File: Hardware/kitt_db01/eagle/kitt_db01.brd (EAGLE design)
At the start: 74.3 x 53.3 mm, 25 parts, among them Q1 [MMBF170], U1 ADNS-3080, U2 MIC5205-3.3YM5TR, X1 RESON

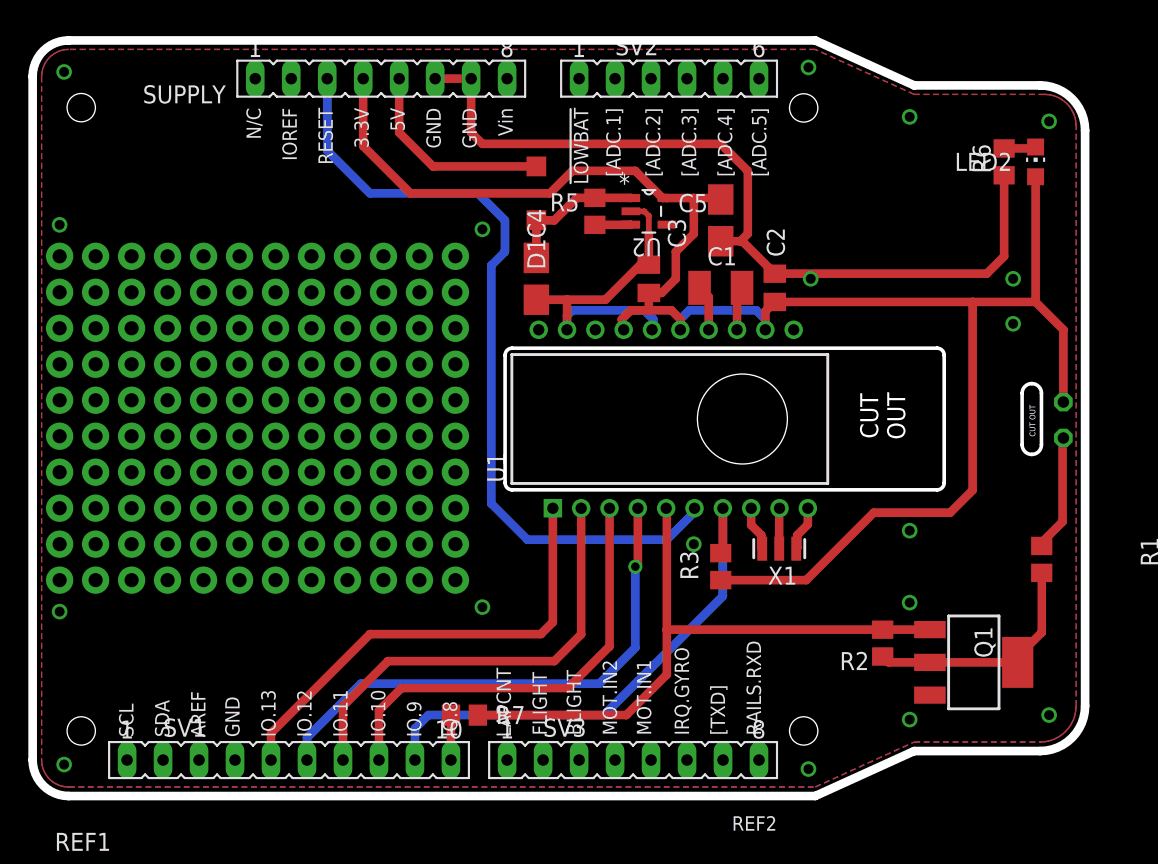
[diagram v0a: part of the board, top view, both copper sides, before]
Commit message: board snapshot of db01 + added patching area for north-west port
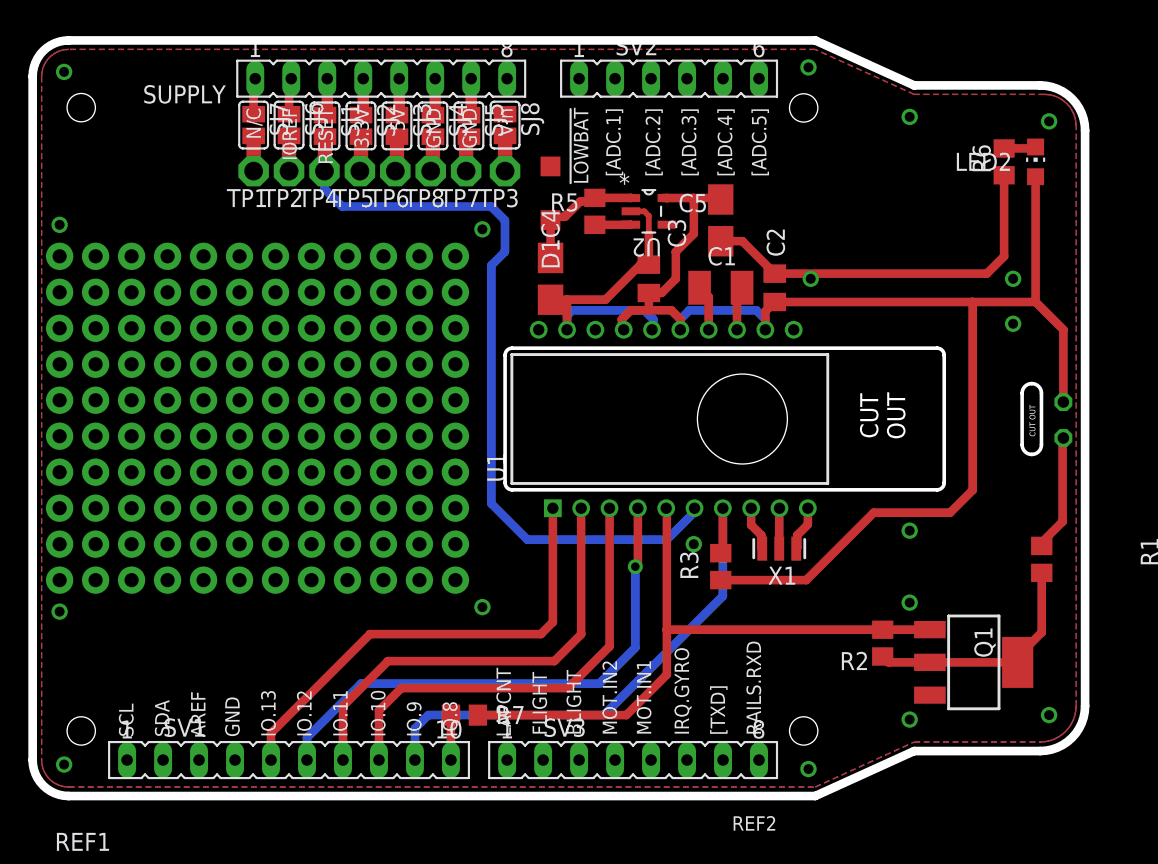
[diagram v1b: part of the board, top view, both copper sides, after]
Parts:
- added SJ1, SJ2, SJ3, SJ4, SJ5, SJ6, SJ7, SJ8: (no value), jumper:SJ
- added TP1, TP2, TP3, TP4, TP5, TP6, TP7, TP8: TPPAD1-13, testpad:P1-13
- moved C4 1.00 mm to (30.2, 68.9)
- moved D1 1.00 mm to (30.2, 74.9)
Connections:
- new net N$12: SJ1.1, SUPPLY.3
- new net N$13: SJ2.1, SUPPLY.4
- new net N$134: SJ3.1, SUPPLY.5
- new net N$135: SJ4.1, SUPPLY.6
- new net N$136: SJ5.1, SUPPLY.7
- new net N$137: SJ7.1, SUPPLY.1
- new net N$138: SJ6.1, SUPPLY.2
- new net N$139: SJ8.1, SUPPLY.8
- new net N$140: SJ7.2, TP1.TP
- new net N$141: SJ6.2, TP2.TP
- new net N$142: SJ8.2, TP3.TP
- net +3V3: now also SJ2.2, TP5.TP; no longer SUPPLY.4
- net +5V: now also SJ3.2, TP6.TP; no longer SUPPLY.5
- net GND: now also SJ4.2, SJ5.2, TP7.TP, TP8.TP; no longer SUPPLY.6, SUPPLY.7
- net RST: now also SJ1.2, TP4.TP; no longer SUPPLY.3
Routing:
- net GND: track 83.6 -> 55.1 mm
- net +3V3: track 128.3 -> 102.1 mm
- net +5V: track 14.5 -> 2.48 mm
- net N$135: track 0.00 -> 2.64 mm
- net N$134: track 0.00 -> 2.64 mm
- net N$12: track 0.00 -> 2.64 mm
- net N$136: track 0.00 -> 2.64 mm
- net N$13: track 0.00 -> 2.64 mm
- net N$138: track 0.00 -> 2.58 mm
- net N$137: track 0.00 -> 2.56 mm
- net N$142: track 0.00 -> 2.49 mm
- net N$141: track 0.00 -> 2.49 mm
- net N$140: track 0.00 -> 2.49 mm
- net RST: track 56.5 -> 54.3 mm
- net N$9: track 9.99 -> 8.99 mm
- added copper zone on layer 3, net GND

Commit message: snapshot of board db01 + added southwest patching area
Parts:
- added SJ10, SJ11, SJ12, SJ13, SJ14, SJ15, SJ16, SJ17, SJ18, SJ19, SJ9: (no value), jumper:SJ
- added TP10, TP11, TP12, TP13, TP14, TP15, TP16, TP17, TP18, TP9: TPPAD1-13, testpad:P1-13
- moved R7 5.25 mm to (29.4, 38.1)
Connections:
- new net N$143: SJ9.1, SV1.1
- new net N$144: SJ10.1, SV1.2
- new net N$145: SJ11.1, SV1.3
- new net N$146: SJ11.2, TP9.TP
- new net N$147: SJ12.1, SV1.4
- new net N$148: SJ13.1, SV1.5
- new net N$149: SJ14.1, SV1.6
- new net N$150: SJ15.1, SV1.7
- new net N$151: SJ16.1, SV1.8
- new net N$152: SJ17.1, SV1.9
- new net N$153: SJ18.1, SV1.10
- new net SCL: SJ9.2, TP11.TP
- new net SDA: SJ10.2, TP10.TP
- net !CS: now also SJ13.2, TP12.TP; no longer SV1.5
- net !LEDCTRL: now also SJ18.2, TP17.TP; no longer SV1.10
- net !PD: now also SJ17.2, TP16.TP; no longer SV1.9
- net GND: now also SJ12.2, TP18.TP; no longer SV1.4
- net MISO: now also SJ15.2, TP14.TP; no longer SV1.7
- net MOSI: now also SJ14.2, TP13.TP; no longer SV1.6
- net SCLK: now also SJ16.2, TP15.TP; no longer SV1.8
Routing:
- net MOSI: track 37.3 -> 15.7 mm
- net MISO: track 31.6 -> 13.8 mm
- net SCLK: track 31.4 -> 16.2 mm
- net !PD: track 37.3 -> 24.9 mm
- net !CS: track 33.1 -> 23.5 mm
- net N$4: track 44.9 -> 39.6 mm
- net N$153: track 0.00 -> 2.64 mm
- net N$152: track 0.00 -> 2.62 mm
- net N$144: track 0.00 -> 2.61 mm
- net N$145: track 0.00 -> 2.61 mm
- net N$151: track 0.00 -> 2.60 mm
- net N$143: track 0.00 -> 2.59 mm
- net N$147: track 0.00 -> 2.59 mm
- net N$150: track 0.00 -> 2.59 mm
- net N$139: track 0.00 -> 2.57 mm
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
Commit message: snapshot of db01 board -> added northeast and southeast patchthough to pins
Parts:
- added SJ20, SJ21, SJ22, SJ23, SJ24, SJ25, SJ26, SJ27, SJ28, SJ29, SJ30, SJ31, SJ32, SJ33: (no value), jumper:SJ
- added TP19, TP20, TP21, TP22, TP23, TP24, TP25, TP26, TP27, TP28, TP29, TP30, TP31, TP32: TPPAD1-13, testpad:P1-13
- moved SJ19 16.8 mm to (65.2, 28.0)
- moved R7 8.07 mm to (31.6, 45.9)
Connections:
- new net N$154: SJ20.1, SV2.6
- new net N$155: SJ21.1, SV2.5
- new net N$156: SJ22.1, SV2.4
- new net N$157: SJ23.1, SV2.3
- new net N$158: SJ24.1, SV2.2
- new net N$159: SJ25.1, SV2.1
- new net N$160: SJ26.1, SV3.8
- new net N$161: SJ27.1, SV3.7
- new net N$162: SJ28.1, SV3.6
- new net N$163: SJ29.1, SV3.5
- new net N$164: SJ30.1, SV3.4
- new net N$165: SJ31.1, SV3.3
- new net N$166: SJ32.1, SV3.2
- new net N$167: SJ33.1, SV3.1
- new net N$168: SJ20.2, TP19.TP
- new net N$169: SJ21.2, TP20.TP
- new net N$170: SJ22.2, TP21.TP
- new net N$171: SJ23.2, TP22.TP
- new net N$172: SJ24.2, TP23.TP
- new net N$173: SJ25.2, TP24.TP
- new net N$174: SJ26.2, TP25.TP
- new net N$175: SJ27.2, TP26.TP
- new net N$176: SJ28.2, TP27.TP
- new net N$177: SJ29.2, TP28.TP
- new net N$178: SJ30.2, TP29.TP
- new net N$179: SJ31.2, TP30.TP
- new net N$180: SJ32.2, TP31.TP
- new net N$181: SJ33.2, TP32.TP
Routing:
- net !CS: track 23.5 -> 2.24 mm
- net SCLK: track 16.2 -> 2.24 mm
- net N$4: track 39.6 -> 27.2 mm
- net !PD: track 24.9 -> 13.0 mm
- net MISO: track 13.8 -> 2.24 mm
- net MOSI: track 15.7 -> 6.43 mm
- net N$160: track 0.00 -> 2.64 mm
- net N$161: track 0.00 -> 2.62 mm
- net N$167: track 0.00 -> 2.61 mm
- net N$162: track 0.00 -> 2.60 mm
- net N$166: track 0.00 -> 2.59 mm
- net N$154: track 0.00 -> 2.59 mm
- net N$163: track 0.00 -> 2.59 mm
- net N$165: track 0.00 -> 2.57 mm
- net N$155: track 0.00 -> 2.57 mm
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
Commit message: snapshot of db01 board layout -> added alternate LEDs for illuminating surface
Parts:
- removed Q1: [MMBF170], transistor-power:SOT223
- removed SJ19: (no value), jumper:SJ
- added LED3, LED4, LED5: (no value), led:CHIP-LED0805
- added R10, R9: 330R, rcl:R0805
- added R4: [0R], rcl:R0805
- added U9.01: SI1922EDH, kitt.ic:SC70-6
- moved R2 11.0 mm to (61.0, 51.4)
- moved R7 5.10 mm to (36.5, 47.3), turned to 270 degrees
- moved R1 2.40 mm to (65.1, 46.7)
- moved R5 1.91 mm to (33.3, 71.8)
- moved R3 1.27 mm to (42.2, 47.3)
- moved U2 1.27 mm to (37.1, 72.4)
- moved C5 0.95 mm to (42.2, 72.1), turned to 180 degrees
- moved LED1 0.63 mm to (65.8, 58.9)
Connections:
- new net N$184: R4.2, U9.01.5
- new net N$185: LED4.C, R9.2
- new net N$186: R10.1, R9.1, U9.01.3
- new net N$187: LED5.C, R10.2
- net !LEDCTRL: now also R4.1
- net +3V3: now also LED3.A, LED4.A, LED5.A
- net GND: now also U9.01.1, U9.01.4; no longer Q1.3
- net MISO: now also SJ14.2, TP13.TP; no longer SJ15.2, TP14.TP
- net MOSI: now also SJ16.2, TP15.TP; no longer SJ14.2, TP13.TP
- net N$4: now also U9.01.2; no longer Q1.1
- net N$7: now also U9.01.6; no longer Q1.2, Q1.4
- net N$8: now also LED3.C
- net SCLK: now also SJ15.2, TP14.TP; no longer SJ16.2, TP15.TP
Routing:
- net +3V3: track 102.1 -> 131.2 mm, vias 0 -> 4
- net !CS: track 2.24 -> 29.3 mm
- net MISO: track 2.24 -> 28.4 mm, vias 0 -> 1
- net SCLK: track 2.24 -> 26.9 mm
- net !PD: track 13.0 -> 36.0 mm
- net MOSI: track 6.43 -> 27.0 mm, vias 1 -> 0
- net N$7: track 16.7 -> 0.00 mm
- net !LEDCTRL: track 2.24 -> 18.8 mm, vias 0 -> 1
- net +5V: track 2.48 -> 16.7 mm
- net GND: track 55.1 -> 41.5 mm, vias 18 -> 15
- net N$4: track 27.2 -> 18.0 mm
- net N$8: track 8.23 -> 1.75 mm
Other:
- board size 74.3 x 53.3 mm -> 133.3 x 98.3 mm
- board text added: "40deg light cone"
- board text added: "80deg light cone"
- board text added: "<-- replace with SMT LED (there's got to be one, no need for shite slot)"
- board text added: "or atleast an alternate footprint"
- board text removed: "The Prototyping Area is here because: - it enables quick bodgejobs - it uses up real estate which would be wasted otherwise"

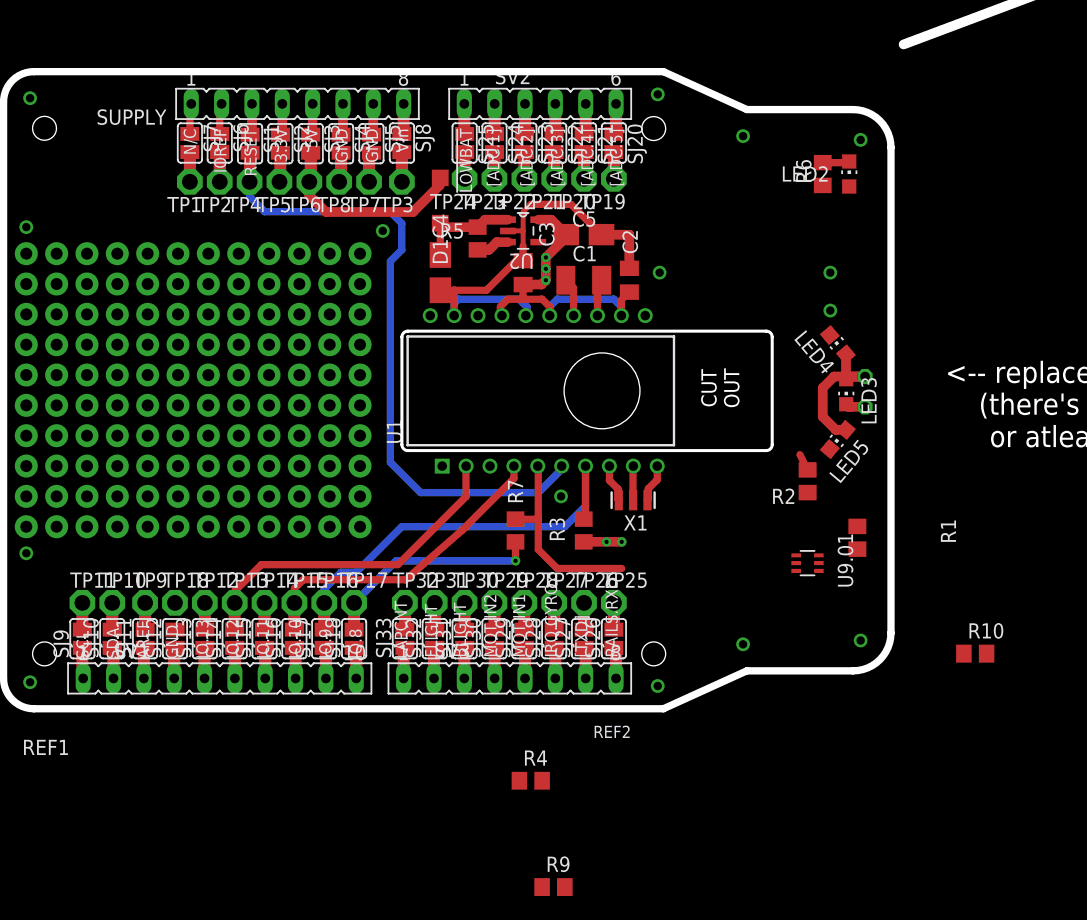
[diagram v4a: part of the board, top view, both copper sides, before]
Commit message: snapshot of db01 board layout : almost done edition -> now exporting BOM for this design -> footprints are all go -> powerplane and grounding to be done after BOM
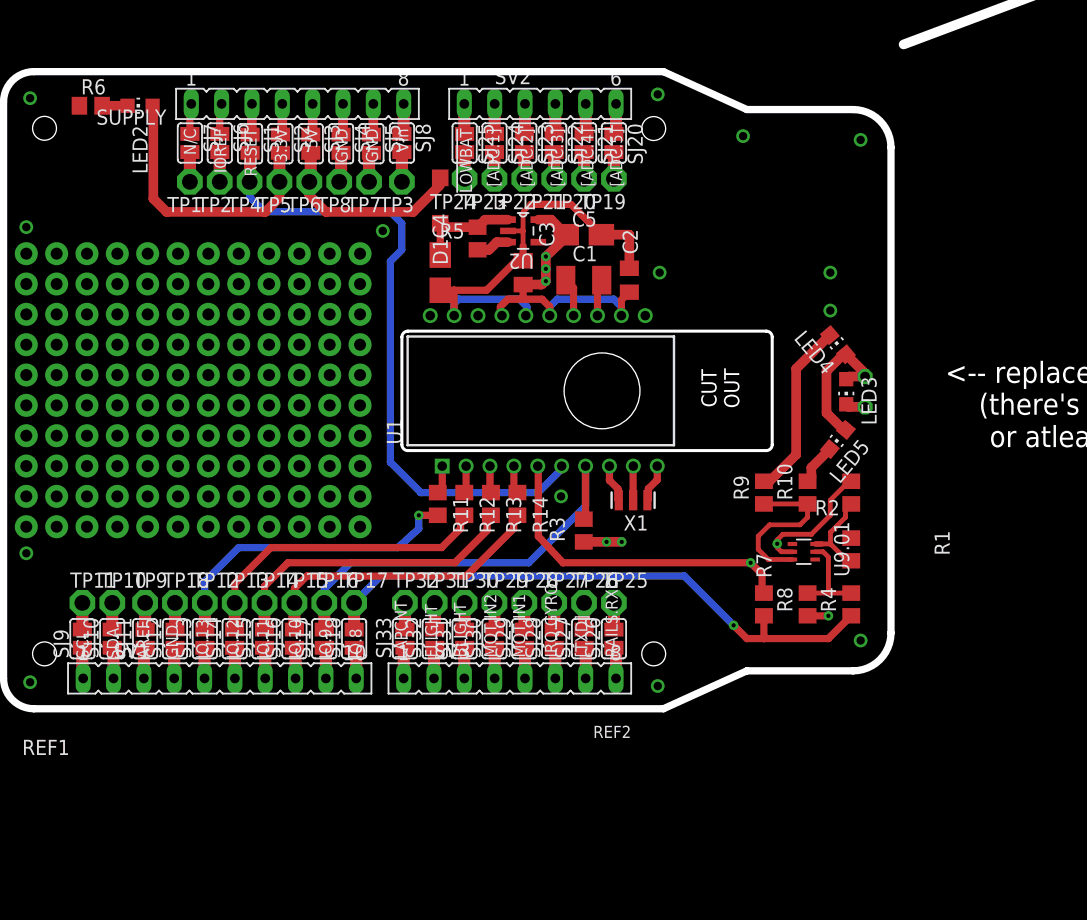
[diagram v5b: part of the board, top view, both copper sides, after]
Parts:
- added R11, R12, R13, R14: [PPR], rcl:R0805
- added R8: [0R], rcl:R0805
- moved R6 61.5 mm to (0.95, 82.9), turned to 180 degrees
- moved LED2 59.6 mm to (5.08, 82.9), turned to 90 degrees
- moved R9 37.4 mm to (57.3, 50.5), turned to 90 degrees
- moved R4 30.6 mm to (64.6, 41.1), turned to 90 degrees
- moved R7 21.7 mm to (57.3, 41.1)
- moved R10 19.5 mm to (61.0, 50.5), turned to 90 degrees
- moved R2 3.77 mm to (64.6, 50.5)
- moved R1 1.12 mm to (64.6, 45.7)
- moved U9.01 1.00 mm to (60.6, 45.5)
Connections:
- new net AUXLED: R8.1, SJ20.2, TP19.TP
- new net N$182: R12.1, U1.2
- new net N$183: R13.1, U1.3
- new net N$188: R14.1, U1.4
- net !CS: now also R11.2; no longer U1.1
- net MISO: now also R12.2; no longer U1.2
- net MOSI: now also R14.2; no longer U1.4
- net N$168: now also R11.1, U1.1; no longer SJ20.2, TP19.TP
- net N$184: now also R8.2
- net SCLK: now also R13.2; no longer U1.3
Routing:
- net AUXLED: track 0.00 -> 55.3 mm, vias 0 -> 1
- net !LEDCTRL: track 18.8 -> 49.7 mm
- net N$4: track 18.0 -> 41.6 mm, vias 0 -> 2
- net +3V3: track 131.2 -> 149.2 mm, vias 4 -> 5
- net N$185: track 0.00 -> 14.8 mm
- net N$186: track 0.00 -> 13.9 mm
- net N$7: track 0.00 -> 8.60 mm
- net N$184: track 0.00 -> 7.97 mm
- net N$187: track 0.00 -> 3.46 mm
- net !CS: track 29.3 -> 26.5 mm, vias 0 -> 1
- net N$188: track 0.00 -> 2.34 mm
- net N$182: track 0.00 -> 2.28 mm, vias 1 -> 0
- net N$183: track 0.00 -> 2.25 mm, vias 1 -> 0
- net GND: track 41.5 -> 43.7 mm, vias 15 -> 14
- net MISO: track 28.4 -> 26.4 mm, vias 1 -> 0
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
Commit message: finished part search for db-01, updated footprints accordingly
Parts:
- removed C1: (no value), rcl:SMC_B
- removed U$1: (no value), frames:A3L-LOC
- removed U2: MIC5205-3.3YM5TR, kitt.ic:SOT95P280X130-5N
- added C9.03: 2.2uF, rcl:C1608
- added U$2: (no value), frames:A4L-LOC
- added U9.02: SI1922EDH, kitt.ic:SC70-6
- D9.00: value POWER -> RED
- D9.01, D9.02: value (none) -> RED
- D9.03, D9.04: value (none) -> GREEN
- U9.01: value SI1922EDH -> MIC5205-3.3YM5TR; device kitt.ic:SC70-6 -> kitt.ic:SOT95P280X130-5N
- moved U9.01 35.7 mm to (37.1, 72.4), turned to 0 degrees
- renumbered C2 to C9.04, C3 to C9.05, C4 to C9.00, C5 to C9.01, D1 to D9.99, LED1 to D9.01, LED2 to D9.00, LED3 to D9.02, LED4 to D9.04, LED5 to D9.03, R1 to R9.08, R10 to R9.09, R11 to R9.02, R12 to R9.03, R13 to R9.04, R14 to R9.05, R2 to R9.06, R3 to R9.01, R4 to R9.11, R5 to R9.00, R6 to R9.13, R7 to R9.07, R8 to R9.12, R9 to R9.10, U1 to U9.00, X1 to X9.00
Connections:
- net +3V3: now also U9.01.5; no longer U2.5
- net GND: now also U9.01.2, U9.02.1, U9.02.4; no longer U2.2, U9.01.1, U9.01.4
- net N$10: now also U9.01.3; no longer U2.3
- net N$184: now also U9.02.5; no longer U9.01.5
- net N$186: now also U9.02.3; no longer U9.01.3
- net N$4: now also U9.02.2; no longer U9.01.2
- net N$5: now also C9.03.1; no longer C1.+
- net N$6: now also C9.03.2; no longer C1.-
- net N$7: now also U9.02.6; no longer U9.01.6
- net N$9: now also U9.01.1; no longer U2.1
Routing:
- net GND: track 43.7 -> 47.4 mm
- added copper zone on layer 2, net GND
- added copper zone on layer 2, net GND1
- removed copper zone on layer 3, net GND
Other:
- board size 133.3 x 98.3 mm -> 74.3 x 53.3 mm
- board text removed: "40deg light cone"
- board text removed: "80deg light cone"
- board text removed: "<-- replace with SMT LED (there's got to be one, no need for shite slot)"
- board text removed: "or atleast an alternate footprint"
